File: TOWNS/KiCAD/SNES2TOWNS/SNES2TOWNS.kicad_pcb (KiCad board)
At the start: 2 copper layers, 12 parts, among them J1 DE9_Receptacle, J6 SNES_CONTROLLER, J7 Slide Switch, J8 ArduinoNANOP1_P15, J9 ArduinoNANOP16_P30, U1 74LS157, U2 74LS157

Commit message: Optimizing PCB
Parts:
- moved R2 8.35 mm to (117.3, 98.5)
- moved J1 6.99 mm to (159.4, 76.5)
- moved U2 3.97 mm to (144.7, 91.1)
- moved U1 3.68 mm to (144.8, 67.3)
- moved R1 3.05 mm to (118.9, 103.1)
- moved C2 2.77 mm to (140.1, 92.7)
- moved J7 2.01 mm to (160.8, 105.8)
- moved C1 1.78 mm to (141.1, 74.7), turned to 0 degrees
- moved R3 1.62 mm to (162.3, 99.2)
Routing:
- net /COM: track 81.4 -> 56.2 mm
- net /OUT_P1: track 36.6 -> 16.3 mm
- net /OUT_P4A: track 53.6 -> 36.6 mm
- net /OUT_P6: track 61.0 -> 44.7 mm
- net /TWNS2BTN: track 107.9 -> 96.9 mm
- net /OUT_P7: track 48.9 -> 53.6 mm
- net /OUT_P6A: track 13.6 -> 9.44 mm
- net /OUT_P6B: track 13.5 -> 9.44 mm
- net +5V: track 137.9 -> 134.2 mm
- net /OUT_P4B: track 39.5 -> 35.8 mm
- net /OUT_P3B: track 20.5 -> 16.8 mm
- net /OUT_P2A: track 12.9 -> 9.20 mm
- net /OUT_P1B: track 11.8 -> 8.15 mm
- net /OUT_P1A: track 30.0 -> 26.3 mm
- net /OUT_P3A: track 20.5 -> 16.8 mm
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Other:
- board outline added: 68.6 x 50.8 mm
- board text added: "SNES Game Controller to FM TOWNS Adapter Ver. 20230903 by CaptainYS http://www.ysflight.com"
- board text removed: "SNES Game Controller to FM TOWNS Adapter Ver. 20230901 by CaptainYS http://www.ysflight.com"

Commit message: PCB
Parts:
- J6: footprint Connector_PinHeader_2.54mm:PinHeader_1x07_P2.54mm_Vertical -> SNES:SNES_Controller
- moved R2 12.2 mm to (115.6, 110.6)
- moved R1 7.49 mm to (119.0, 110.6)
- moved J6 5.92 mm to (112.3, 71.1), turned to -90 degrees
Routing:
- net +5V: track 134.2 -> 157.9 mm
- net GND: track 194.7 -> 214.7 mm
- net /CLOCK: track 0.00 -> 18.8 mm
- net /LATCH: track 0.00 -> 18.0 mm
- net /DATA: track 0.00 -> 16.0 mm
- net /TWNS2BTN: track 96.9 -> 109.7 mm
- net /TWNS6BTN: track 103.4 -> 110.3 mm
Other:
- board size 68.6 x 50.8 mm -> 64.8 x 50.8 mm

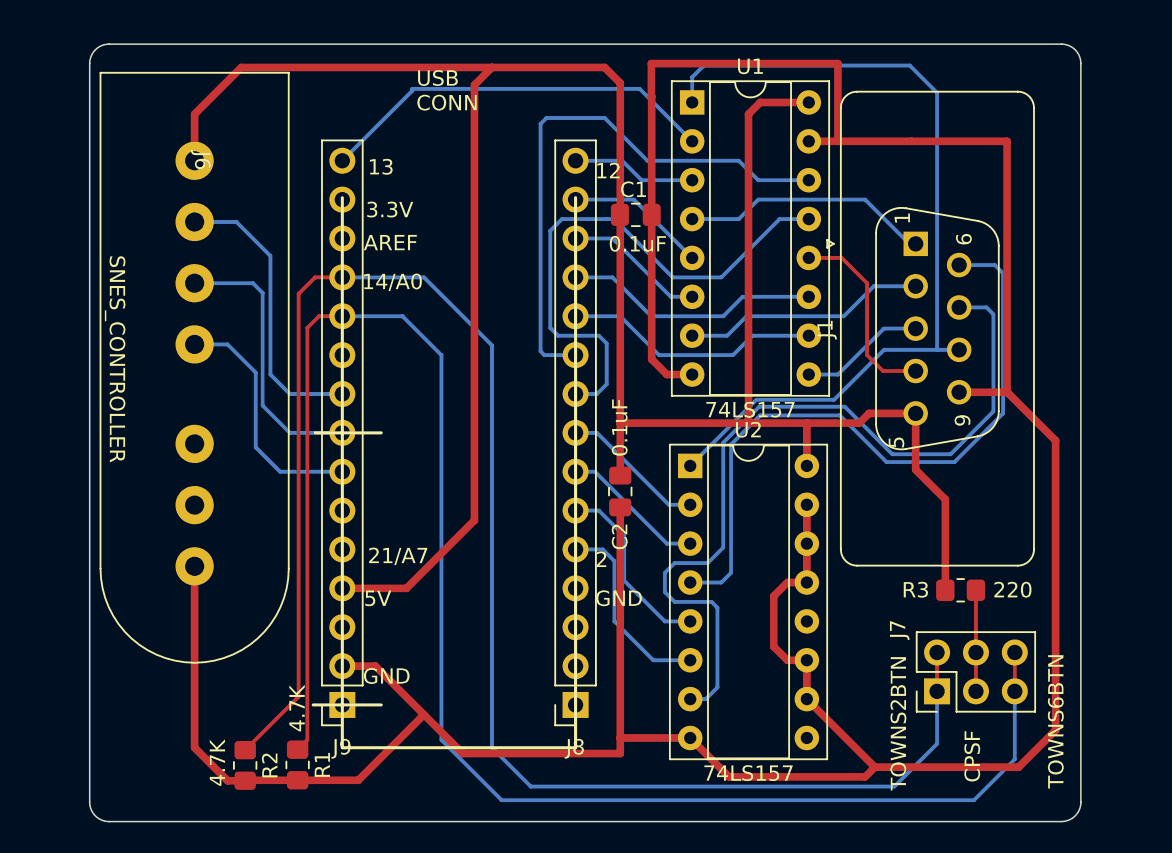
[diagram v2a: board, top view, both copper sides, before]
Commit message: Added status LED.
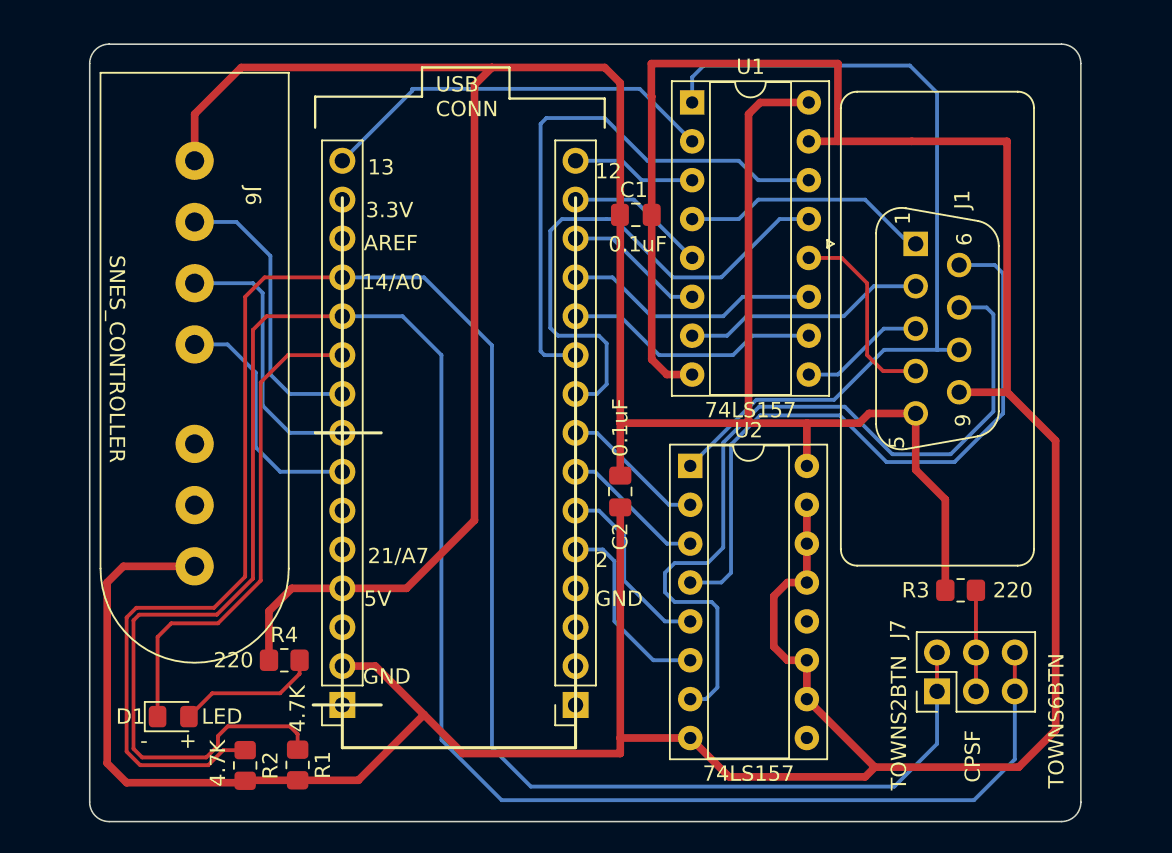
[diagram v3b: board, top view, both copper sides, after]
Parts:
- added D1: LED, LED_SMD:LED_0805_2012Metric_Pad1.15x1.40mm_HandSolder, F.Cu at (110.9, 107.4)
- added R4: 220, Resistor_SMD:R_0805_2012Metric_Pad1.20x1.40mm_HandSolder, F.Cu at (118.1, 103.8)
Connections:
- J9 pad 10: unconnected-(J9-Pin_10-Pad10) -> Net-(D1-K)
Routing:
- net Net-(D1-K): track 0.00 -> 32.5 mm
- net /TWNS6BTN: track 110.3 -> 133.1 mm
- net /TWNS2BTN: track 109.7 -> 126.5 mm
- net GND: track 214.7 -> 226.2 mm
- net Net-(D1-A): track 0.00 -> 9.28 mm
- net +5V: track 157.9 -> 166.5 mm
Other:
- board text added: "+"
- board text added: "-"
